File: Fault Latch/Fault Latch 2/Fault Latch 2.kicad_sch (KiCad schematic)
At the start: 111 parts, among them K102 Fujitsu_FTR-LYAA005x, K103 Fujitsu_FTR-LYAA005x, K104 Fujitsu_FTR-LYAA005x, Q102 Q_NMOS_GSD, Q104 Q_NPN_BEC, Q105 Q_PMOS_GSD, Q106 Q_NPN_BEC, Q107 Q_NPN_BEC, Q108 Q_NPN_BEC, Q109 Q_PMOS_GSD, Q110 Q_PMOS_GSD, Q111 Q_NMOS_GDS, Q112 Q_NPN_BEC, Q113 Q_NPN_BEC, Q114 Q_NMOS_GDS, Q115 Q_NMOS_GSD, Q116 Q_NMOS_GSD, Q117 Q_NMOS_GDS, Q118 Q_PMOS_GSD, SW101 SW_Omron_B3FS, SW102 SW_Omron_B3FS, SW103 SW_Omron_B3FS, U101 641964-1, U102 74AHC1G00, U103 74AHC1G00, U104 74AHC1G00, U105 641964-1, U106 74LS279, U111 641964-1, U112 641964-1, U113 641964-1, U114 SFH617A-1, U115 SFH617A-1, U116 SFH617A-1, U117 641964-1, U118 LM555xM, U119 641964-1, U120 74AHC1G08, U121 641964-1, U122 641964-1, U125 SFH617A-1, U126 SFH617A-1, U127 SFH617A-1

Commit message: Fault Latch V2.0 waiting for final check
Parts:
- removed D1, D2, D3, D4: US2AA, Diode_SMD:D_SMA, symbol Diode:US2AA
- added D110, D111, D112, D113: D_Schottky, Diode_SMD:D_SMA, symbol Device:D_Schottky
- added Q103: Q_NMOS_GSD, Package_TO_SOT_SMD:SOT-23, symbol Transistor_FET:Q_NMOS_GSD
- added R117: 500R, Resistor_SMD:R_0603_1608Metric, symbol Device:R_US
- C116: JLC# (none) -> C2929204
- R111: JLC# (none) -> C22809
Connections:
- net +12V: now also R117.1
- net BMS_Green: now also D110.2 (A)
- net GNDPWR: now also Q103.2 (S)
- net IMD_Green: now also D111.2 (A)
- net IMD_LED: now also Q103.1 (G); no longer Q102.1 (G)
- net at U120.1: now also D112.1 (K), D113.1 (K)
- net at Q110.2 (S), R141.1: now also D112.2 (A)
- net at Q116.1 (G), R123.2: now also D110.1 (K), D111.1 (K)
- net at Q118.2 (S), R142.1: now also D113.2 (A)
- new net: Q102.1 (G), Q103.3 (D), R117.2
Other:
- note removed: "Questions: Doesn't the nmos need a resistor on it? In the rules, it says that we can only turn off stuf via cockpit switch READ OVER REULES!!!"
- note removed: "Was a LED but got replaced --->"
- moved on the sheet: C111, C113, C114, C115, C116, C117, H101, H102, H103, H104, Q110, Q115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

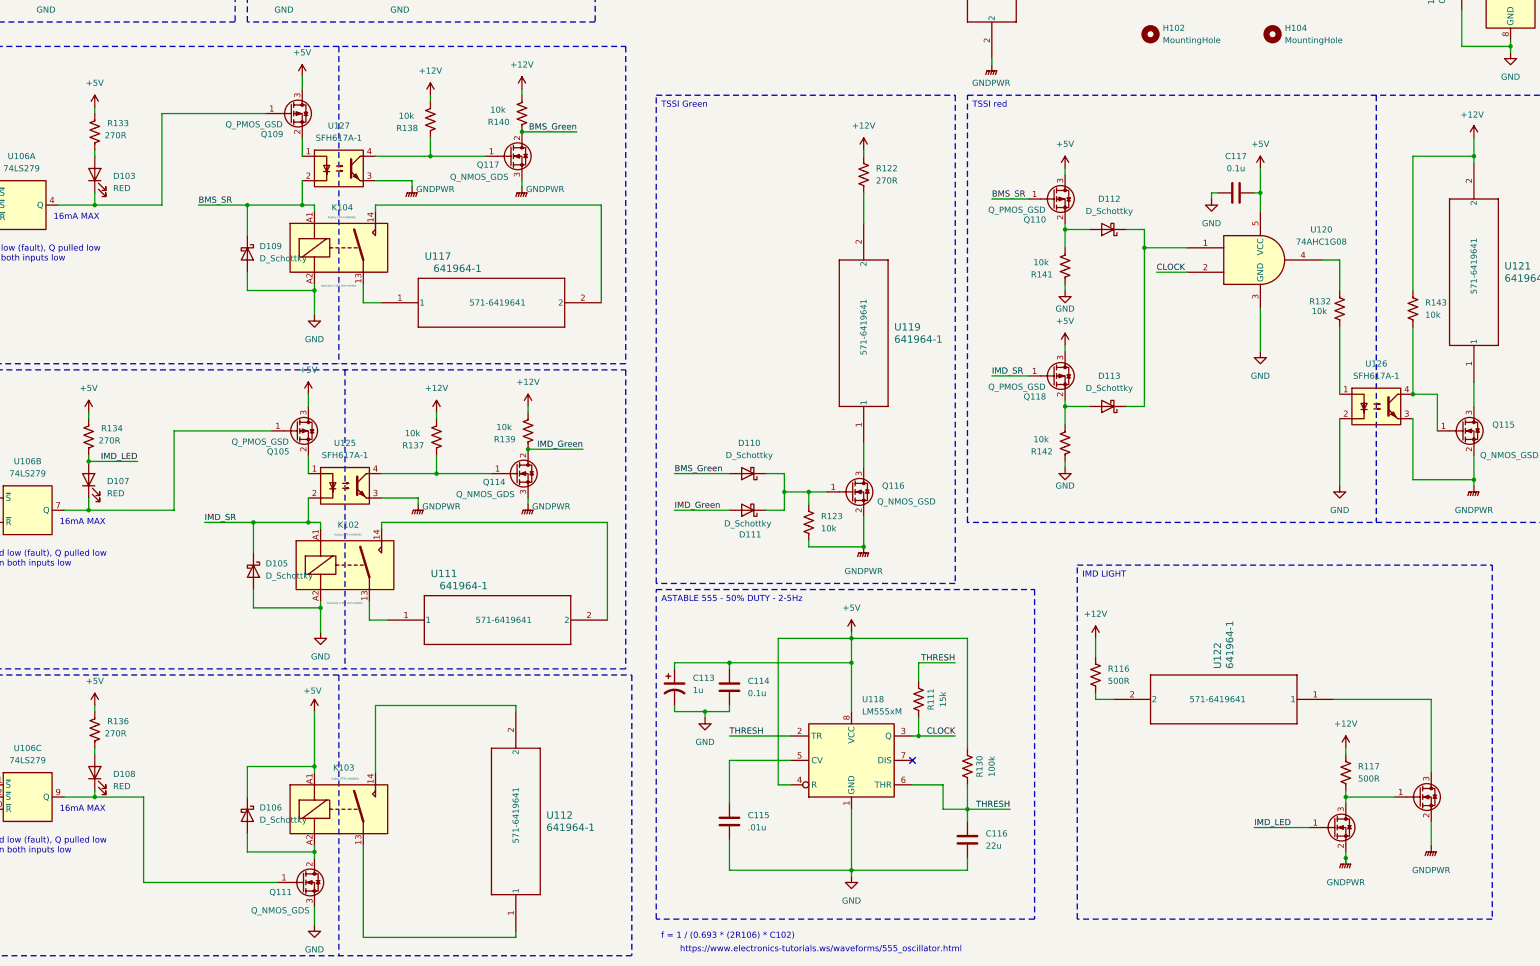
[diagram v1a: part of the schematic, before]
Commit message: BSPD needs to be fixed + Fault Latch Layout Issue
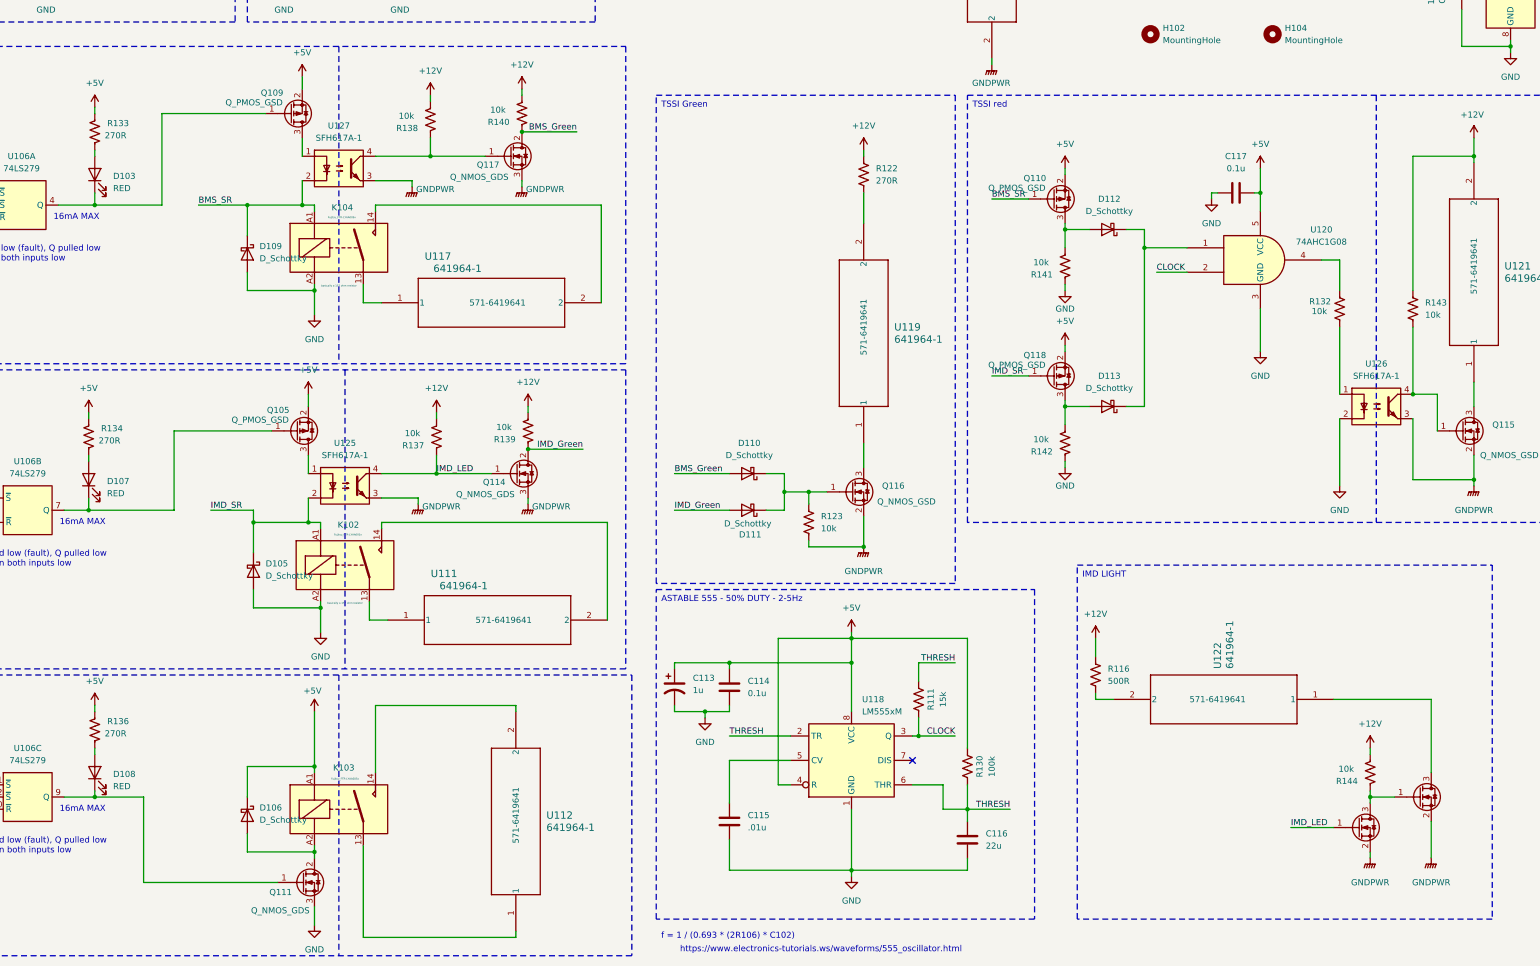
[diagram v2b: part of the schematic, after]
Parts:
- removed R117: 500R, Resistor_SMD:R_0603_1608Metric, symbol Device:R_US
- added R144: 10k, Resistor_SMD:R_0805_2012Metric_Pad1.20x1.40mm_HandSolder, symbol Device:R_US
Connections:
- net +12V: now also R144.1
- net +5V: now also Q105.2 (S), Q109.2 (S), Q110.2 (S), Q118.2 (S); no longer Q105.3 (D), Q109.3 (D), Q110.3 (D), Q118.3 (D)
- net IMD_LED: now also Q114.1 (G), R137.2, U125.4; no longer D107.2 (A), R134.1
- net at U125.1: now also Q105.3 (D); no longer Q105.2 (S)
- net at Q102.1 (G), Q103.3 (D): now also R144.2
- net at D112.2 (A), R141.1: now also Q110.3 (D); no longer Q110.2 (S)
- net at D113.2 (A), R142.1: now also Q118.3 (D); no longer Q118.2 (S)
- net at U127.1: now also Q109.3 (D); no longer Q109.2 (S)
- new net: D107.2 (A), R134.1

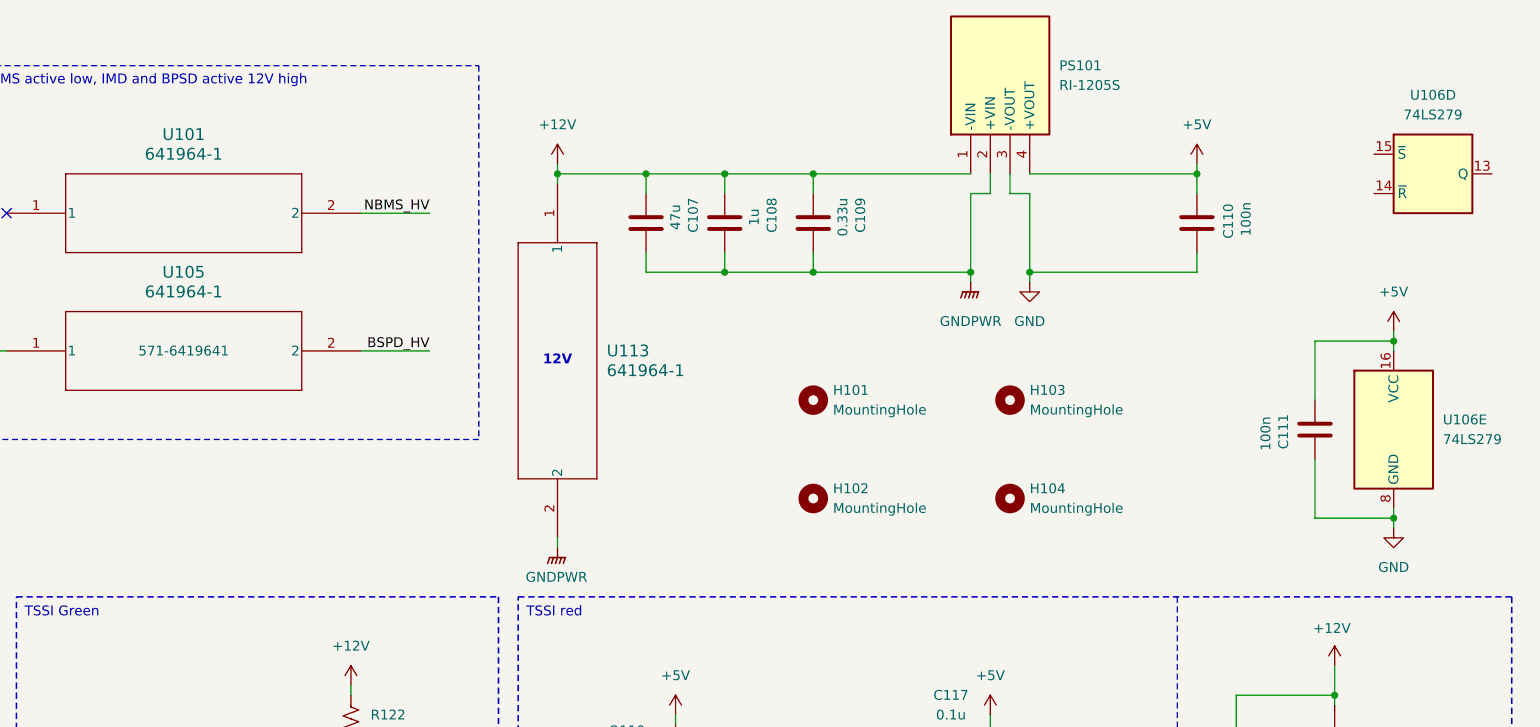
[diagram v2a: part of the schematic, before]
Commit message: Fault latch added Logo
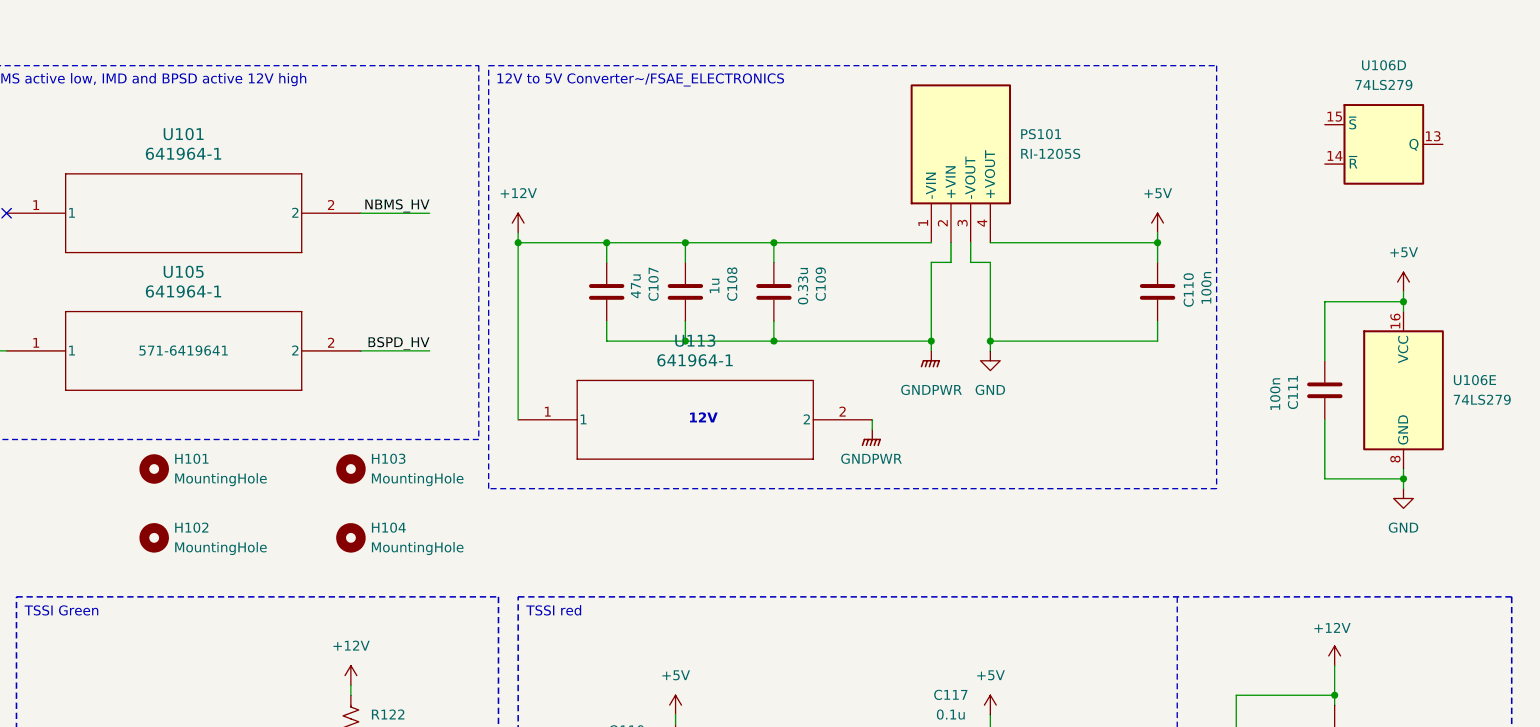
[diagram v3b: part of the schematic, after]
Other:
- moved on the sheet: C107, C108, C109, C110, C111, H101, H102, H103, H104, PS101, U106D, U106E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

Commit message: FAULT LATCH CHANGES
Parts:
- removed D112, D113: D_Schottky, Diode_SMD:D_SMA, symbol Device:D_Schottky
- removed Q110, Q118: Q_PMOS_GSD, Package_TO_SOT_SMD:SOT-523, symbol Transistor_FET:Q_PMOS_GSD
- removed Q114, Q117: Q_NMOS_GDS, Package_TO_SOT_SMD:TO-252-2, symbol Transistor_FET:Q_NMOS_GDS
- removed Q115: Q_NMOS_GSD, Package_TO_SOT_SMD:SOT-23, symbol Transistor_FET:Q_NMOS_GSD
- removed R139, R140, R141, R142: 10k, Resistor_SMD:R_0805_2012Metric_Pad1.20x1.40mm_HandSolder, symbol Device:R_US
- removed U120: 74AHC1G08, Package_TO_SOT_SMD:SOT-353_SC-70-5, symbol 74xGxx:74AHC1G08
- added C112: 0.1u, Capacitor_SMD:C_0402_1005Metric, symbol Device:C
- added Q113: Q_PMOS_GSD, Package_TO_SOT_SMD:SOT-523, symbol Transistor_FET:Q_PMOS_GSD
- added U117, U119: 74AHC1G00, Package_TO_SOT_SMD:SOT-23-5, symbol 74xGxx:74AHC1G00
- renumbered C113 to C107, C114 to C108, C115 to C109, C117 to C110, C116 to C111, C107 to C113, C108 to C114, C109 to C115, C110 to C116, C111 to C117, D107 to D101, D103 to D102, D108 to D103, D109 to D104, D106 to D105, D105 to D106, D110 to D107, D111 to D108, K104 to K101, K103 to K102, K102 to K103, Q104 to Q101, Q106 to Q102, Q107 to Q103, Q108 to Q104, Q103 to Q105, Q102 to Q106, Q109 to Q107, Q105 to Q108, Q111 to Q109, Q112 to Q110, Q113 to Q111, Q116 to Q112, R129 to R102, R131 to R103, R135 to R104, R102 to R105, R107 to R106, R105 to R107, R106 to R108, R104 to R109, R108 to R110, R109 to R111, R116 to R112, R112 to R113, R113 to R114, R114 to R115, R134 to R116, R133 to R117, R136 to R118, R115 to R119, R144 to R121, R124 to R122, R125 to R123, R126 to R124, R138 to R125, R137 to R126, R123 to R128, R128 to R129, R122 to R130, R111 to R131, R130 to R132, R132 to R133, R143 to R134, U114 to U101, U115 to U102, U116 to U103, U102 to U104, U103 to U105, U104 to U106, U106 to U107, U122 to U108, U127 to U109, U125 to U110, U117 to U111, U111 to U112, U112 to U113, U119 to U114, U101 to U115, U105 to U116, U113 to U120, U126 to U121, U121 to U122
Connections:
- net IMD_Green is gone; now on net IMD_LED: D108.2 (A)
- net +12V: now also Q113.2 (S); no longer U122.2
- net +5V: now also C110.2, U121.1, C112.2, U117.5 (VCC), U119.5 (VCC); no longer C110.1
- net BMS_Green: now also R125.2, U109.4
- net BMS_SR: now also D102.1 (K), Q107.1 (G), U107.4 (Q), U117.2; no longer D104.1 (K), K101.A1, U109.2
- net CLOCK: now also U119.2
- net GND: now also C110.1, C112.1, U117.3 (GND), U119.3 (GND); no longer C110.2, U121.2
- net GNDPWR: now also U122.1
- net IMD_SR: now also D101.1 (K), Q108.1 (G), U107.7 (Q), U117.1; no longer D106.1 (K), K103.A1, U110.2
- net at R133.1: now also U121.2
- net at R133.2: now also U119.4; no longer U121.1
- net at R134.2, U121.4: now also Q113.1 (G)
- new net: D106.1 (K), K103.A1, U110.2
- new net: Q113.3 (D), U122.2
- new net: U117.4, U119.1
- new net: D104.1 (K), K101.A1, U109.2
- no-connect marks 2 -> 5
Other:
- moved on the sheet: C101, C102, C103, C104, C105, C106, C107, C108, C109, C110, C111, C113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

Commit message: generated gerber files
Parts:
- C111: JLC# C2929204 -> C105226
- C114: JLC# C1712 -> C91186
- U101, U102, U103, U107, U108, U109, U110, U111, U112, U113, U114, U115, U116, U120, U121, U122: now not fitted
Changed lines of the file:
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@@
 		(in_bom yes)
 		(on_board yes)
-		(dnp no)
+		(dnp yes)
 		(fields_autoplaced yes)
 		(property "Reference" "U107"
@@
 		(in_bom yes)
 		(on_board yes)
-		(dnp no)
+		(dnp yes)
 		(fields_autoplaced yes)
 		(property "Reference" "U101"
@@
 		(in_bom yes)
 		(on_board yes)
-		(dnp no)
+		(dnp yes)
 		(property "Reference" "U112"
 			(at 215.138 197.358 0)
@@
 		(in_bom yes)
 		(on_board yes)
-		(dnp no)
+		(dnp yes)
 		(fields_autoplaced yes)
 		(property "Reference" "U121"
@@
 		(in_bom yes)
 		(on_board yes)
-		(dnp no)
+		(dnp yes)
 		(fields_autoplaced yes)
 		(property "Reference" "U107"
@@
 		(in_bom yes)
 		(on_board yes)
-		(dnp no)
+		(dnp yes)
 		(property "Reference" "U108"
 			(at 126.9999 302.26 90)
@@
 		(in_bom yes)
 		(on_board yes)
-		(dnp no)
+		(dnp yes)
 		(property "Reference" "U111"
 			(at 213.868 128.778 0)
@@
 		(in_bom yes)
 		(on_board yes)
-		(dnp no)
+		(dnp yes)
 		(property "Reference" "U114"
 			(at 237.49 328.9299 90)
@@
 		(in_bom yes)
 		(on_board yes)
-		(dnp no)
+		(dnp yes)
 		(property "Reference" "U122"
 			(at 373.38 237.4899 90)
@@
 		(in_bom yes)
 		(on_board yes)
-		(dnp no)
+		(dnp yes)
 		(property "Reference" "U113"
 			(at 233.68 248.9199 90)
@@
 		(in_bom yes)
 		(on_board yes)
-		(dnp no)
+		(dnp yes)
 		(property "Reference" "U116"
 			(at 287.02 110.49 0)
@@
 		(in_bom yes)
 		(on_board yes)
-		(dnp no)
+		(dnp yes)
 		(fields_autoplaced yes)
 		(property "Reference" "U102"
@@
 		(in_bom yes)
 		(on_board yes)
-		(dnp no)
+		(dnp yes)
 		(property "Reference" "U107"
 			(at 267.97 58.42 0)
@@
 		(in_bom yes)
 		(on_board yes)
-		(dnp no)
+		(dnp yes)
 		(fields_autoplaced yes)
 		(property "Reference" "U103"
@@
 		(in_bom yes)
 		(on_board yes)
-		(dnp no)
+		(dnp yes)
 		(fields_autoplaced yes)
 		(property "Reference" "U109"
@@
 			)
 		)
-		(property "JLC#" "C2929204"
+		(property "JLC#" "C105226"
 			(at 320.04 332.74 0)
 			(effects
@@
 		(in_bom yes)
 		(on_board yes)
-		(dnp no)
+		(dnp yes)
 		(fields_autoplaced yes)
 		(property "Reference" "U120"
@@
 		(in_bom yes)
 		(on_board yes)
-		(dnp no)
+		(dnp yes)
 		(fields_autoplaced yes)
 		(property "Reference" "U110"
@@
 		(in_bom yes)
 		(on_board yes)
-		(dnp no)
+		(dnp yes)
 		(fields_autoplaced yes)
 		(property "Reference" "U107"
@@
 		(in_bom yes)
 		(on_board yes)
-		(dnp no)
+		(dnp yes)
 		(fields_autoplaced yes)
 		(property "Reference" "U115"
@@
 			)
 		)
-		(property "JLC#" "C1712"
+		(property "JLC#" "C91186"
 			(at 356.87 113.03 0)
 			(effects
@@
 		(in_bom yes)
 		(on_board yes)
-		(dnp no)
+		(dnp yes)
 		(fields_autoplaced yes)
 		(property "Reference" "U107"

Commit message: FL READY
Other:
- moved on the sheet: D104
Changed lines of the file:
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@@
 	(wire
 		(pts
-			(xy 171.45 118.11) (xy 182.88 118.11)
+			(xy 166.37 118.11) (xy 182.88 118.11)
 		)
 		(stroke
@@
 	(wire
 		(pts
-			(xy 171.45 118.11) (xy 171.45 124.46)
+			(xy 166.37 118.11) (xy 166.37 124.46)
 		)
 		(stroke
@@
 	(wire
 		(pts
-			(xy 185.42 135.89) (xy 171.45 135.89)
+			(xy 185.42 135.89) (xy 166.37 135.89)
 		)
 		(stroke
@@
 	(wire
 		(pts
-			(xy 171.45 135.89) (xy 171.45 132.08)
+			(xy 166.37 135.89) (xy 166.37 132.08)
 		)
 		(stroke
@@
 	(symbol
 		(lib_id "Device:D_Schottky")
-		(at 171.45 128.27 270)
+		(at 166.37 128.27 270)
 		(unit 1)
 		(exclude_from_sim no)
@@
 		(fields_autoplaced yes)
 		(property "Reference" "D104"
-			(at 173.99 126.6824 90)
+			(at 168.91 126.6824 90)
 			(effects
 				(font
@@
 		)
 		(property "Value" "D_Schottky"
-			(at 173.99 129.2224 90)
+			(at 168.91 129.2224 90)
 			(effects
 				(font
@@
 		)
 		(property "Footprint" "Diode_SMD:D_SMA"
-			(at 171.45 128.27 0)
+			(at 166.37 128.27 0)
 			(effects
 				(font
@@
 		)
 		(property "Datasheet" "~"
-			(at 171.45 128.27 0)
+			(at 166.37 128.27 0)
 			(effects
 				(font
@@
 		)
 		(property "Description" "Schottky diode"
-			(at 171.45 128.27 0)
+			(at 166.37 128.27 0)
 			(effects
 				(font
@@
 		)
 		(property "JLC#" "C8678"
-			(at 171.45 128.27 0)
+			(at 166.37 128.27 0)
 			(effects
 				(font
@@
 		)
 		(property "Sim.Device" ""
-			(at 171.45 128.27 0)
+			(at 166.37 128.27 0)
 			(effects
 				(font
@@
 		)
 		(property "Sim.Pins" ""
-			(at 171.45 128.27 0)
+			(at 166.37 128.27 0)
 			(effects
 				(font
@@
 		)
 		(property "Sim.Type" ""
-			(at 171.45 128.27 0)
+			(at 166.37 128.27 0)
 			(effects
 				(font
@@
 		)
 		(property "MOUSER" ""
-			(at 171.45 128.27 0)
+			(at 166.37 128.27 0)
 			(effects
 				(font
@@
 		)
 		(property "Notes" ""
-			(at 171.45 128.27 0)
+			(at 166.37 128.27 0)
 			(effects
 				(font
